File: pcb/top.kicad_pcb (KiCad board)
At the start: 2 copper layers, 186 x 28 mm, 66 parts, among them J1 Conn_01x01, J10 Conn_01x01, J11 Conn_01x01, J2 Conn_01x01, J3 Conn_01x06, J4 Conn_01x01, J5 Conn_01x01, J6 Conn_01x01, J7 Conn_01x01, J8 Conn_01x01, J9 Conn_01x01, Q1 2N7002, Q2 2N7002, Q3 2N7002, Q4 2N7002, U1 L78L05_SOT89, U2 PIC12F629-ISN

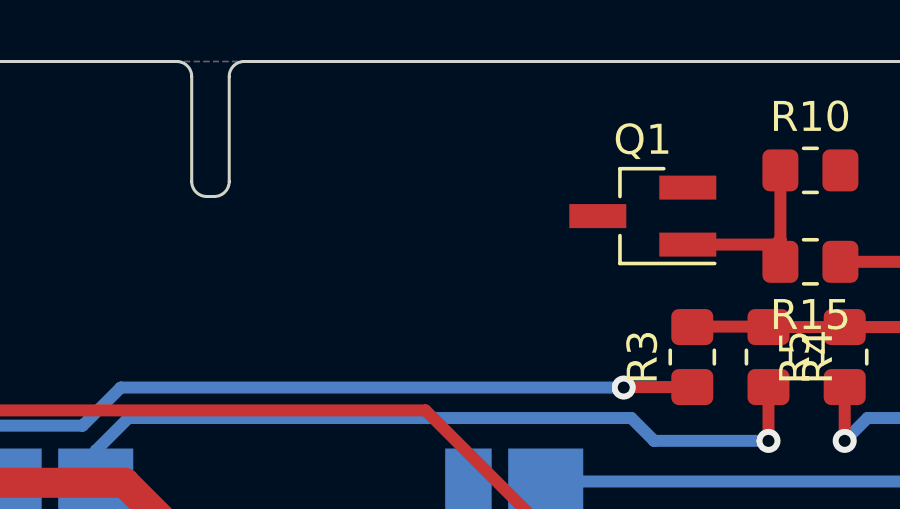
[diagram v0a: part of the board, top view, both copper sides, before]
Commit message: Add load resistor for CV reading.
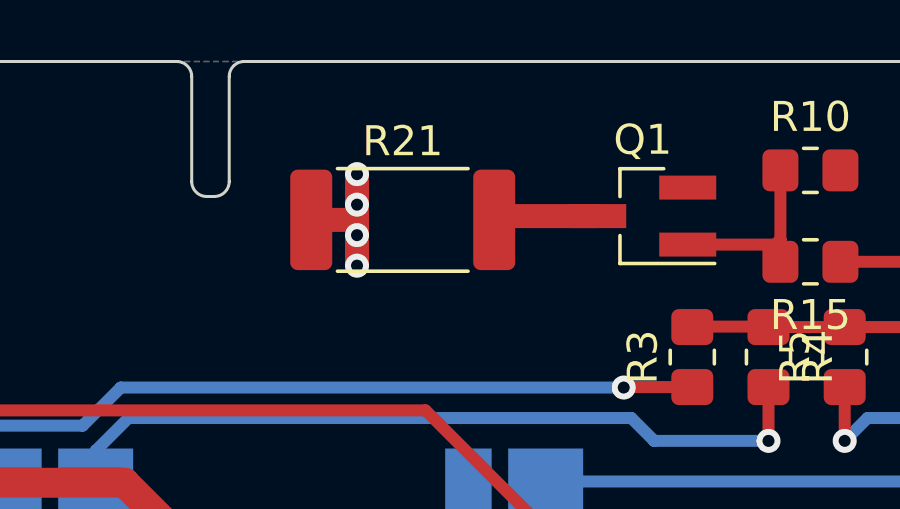
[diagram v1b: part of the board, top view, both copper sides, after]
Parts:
- added R21: 220R, Resistor_SMD:R_2512_6332Metric_Pad1.40x3.35mm_HandSolder, F.Cu at (113.3, 81.3)
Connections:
- Q1 pad 3: unconnected-(Q1-Pad3) -> Net-(Q1-Pad3)
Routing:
- net +15V: track 37.2 -> 41.8 mm, vias 14 -> 18
- net Net-(Q1-Pad3): track 0.00 -> 3.50 mm

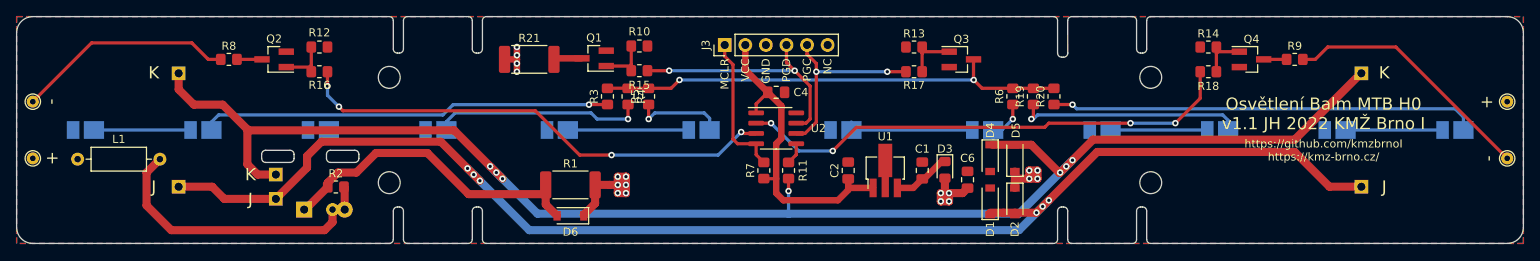
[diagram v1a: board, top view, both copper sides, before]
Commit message: Use 8V stabilized for LEDs.
To keep LEDs longer running on capacitor while maintaining brightness.
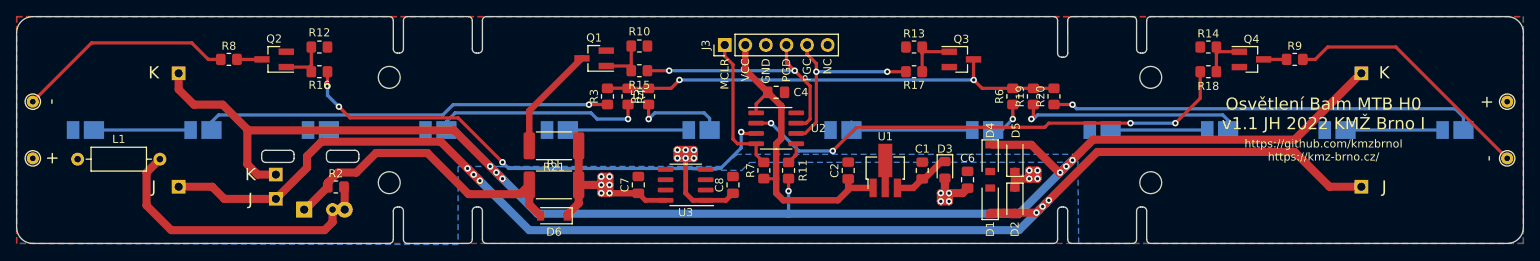
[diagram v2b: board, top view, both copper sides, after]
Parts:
- added C7: 22u/25V, Capacitor_SMD:C_0805_2012Metric_Pad1.18x1.45mm_HandSolder, F.Cu at (126.7, 96.8)
- added C8: 22u/25V, Capacitor_SMD:C_0805_2012Metric_Pad1.18x1.45mm_HandSolder, F.Cu at (138.4, 96.8)
- added U3: L78L08_SO8, Package_SO:SOIC-8_3.9x4.9mm_P1.27mm, F.Cu at (132.6, 96.8)
- R19, R20, R3, R4, R5, R6: value 10k -> 2k2
- moved R21 11.1 mm to (116.3, 91.9), turned to 180 degrees
- moved D6 2.03 mm to (116.3, 100.6)
- moved R1 2.03 mm to (116.3, 96.8)
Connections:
- D11 pad 2: +15V -> +8V
- D12 pad 2: +15V -> +8V
- D15 pad 2: +15V -> +8V
- D16 pad 2: +15V -> +8V
- D7 pad 2: +15V -> +8V
- D8 pad 2: +15V -> +8V
- J6 pad 1: +15V -> +8V
- J7 pad 1: +15V -> +8V
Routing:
- net +8V: track 0.00 -> 20.4 mm, vias 0 -> 6
- net Net-(Q1-Pad3): track 3.50 -> 13.5 mm
- net +15V: track 41.8 -> 48.8 mm, vias 18 -> 14
- net Net-(R16-Pad1): track 60.1 -> 62.6 mm
- net Net-(R2-Pad1): track 39.2 -> 37.9 mm
- added copper zone on B.Cu, net +8V

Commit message: Tweak silkscreen.
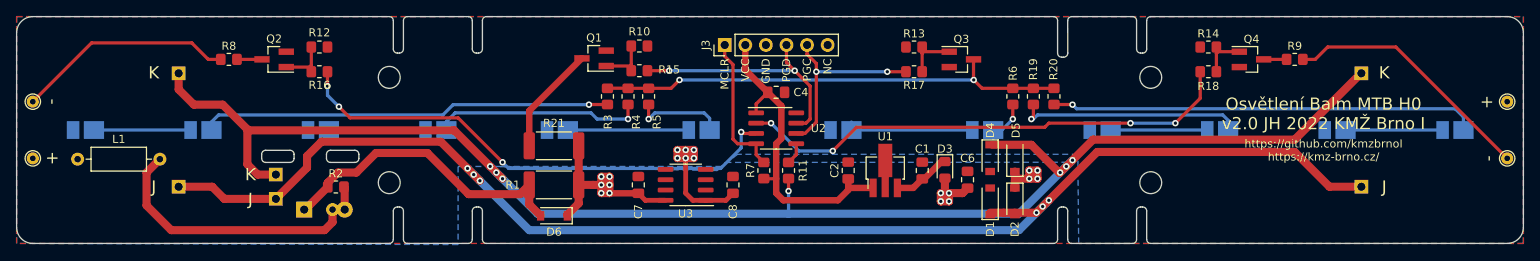
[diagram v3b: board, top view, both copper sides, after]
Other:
- board text added: "Osvětlení Balm MTB H0 v2.0 JH 2022 KMŽ Brno I"
- board text removed: "Osvětlení Balm MTB H0 v1.1 JH 2022 KMŽ Brno I"
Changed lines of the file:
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@@
     (property "Sheetname" "")
     (attr smd)
-    (fp_text reference "R1" (at 0 -2.62) (layer "F.SilkS")
+    (fp_text reference "R1" (at -5.08 0) (layer "F.SilkS")
       (effects (font (size 1 1) (thickness 0.15)))
     )
@@
     (property "Sheetname" "")
     (attr smd)
-    (fp_text reference "R15" (at 0 1.778) (layer "F.SilkS")
+    (fp_text reference "R15" (at 3.683 -0.127) (layer "F.SilkS")
       (effects (font (size 1 1) (thickness 0.15)))
     )
@@
     (property "Sheetname" "")
     (attr smd)
-    (fp_text reference "R4" (at 0 1.651 90) (layer "F.SilkS")
+    (fp_text reference "R4" (at -3.148 1.016 90) (layer "F.SilkS")
       (effects (font (size 1 1) (thickness 0.15)))
     )
@@
     (property "Sheetname" "")
     (attr smd)
-    (fp_text reference "R3" (at 0 -1.65 90) (layer "F.SilkS")
+    (fp_text reference "R3" (at -3.148 0.064 90) (layer "F.SilkS")
       (effects (font (size 1 1) (thickness 0.15)))
     )
@@
     (property "Sheetname" "")
     (attr smd)
-    (fp_text reference "R6" (at 0 -1.65 90) (layer "F.SilkS")
+    (fp_text reference "R6" (at 2.852 0.026 90) (layer "F.SilkS")
       (effects (font (size 1 1) (thickness 0.15)))
     )
@@
     (property "Sheetname" "")
     (attr smd)
-    (fp_text reference "C7" (at 0 -1.68 90) (layer "F.SilkS")
+    (fp_text reference "C7" (at -3.302 0 90) (layer "F.SilkS")
       (effects (font (size 1 1) (thickness 0.15)))
     )
@@
     (property "Sheetname" "")
     (attr smd)
-    (fp_text reference "C8" (at 0 -1.68 90) (layer "F.SilkS")
+    (fp_text reference "C8" (at -3.302 0 90) (layer "F.SilkS")
       (effects (font (size 1 1) (thickness 0.15)))
     )
@@
     (property "Sheetname" "")
     (attr smd)
-    (fp_text reference "R20" (at 0 -1.65 90) (layer "F.SilkS")
+    (fp_text reference "R20" (at 3.352 -0.054 90) (layer "F.SilkS")
       (effects (font (size 1 1) (thickness 0.15)))
     )
@@
     (property "Sheetname" "")
     (attr smd)
-    (fp_text reference "R5" (at 0 -1.65 90) (layer "F.SilkS")
+    (fp_text reference "R5" (at -3.148 1.016 90) (layer "F.SilkS")
       (effects (font (size 1 1) (thickness 0.15)))
     )
@@
     (property "Sheetname" "")
     (attr smd)
-    (fp_text reference "R21" (at 0 -2.62) (layer "F.SilkS")
+    (fp_text reference "R21" (at 0 2.794) (layer "F.SilkS")
       (effects (font (size 1 1) (thickness 0.15)))
     )
@@
     (property "Sheetname" "")
     (attr smd)
-    (fp_text reference "R19" (at 0 -1.65 90) (layer "F.SilkS")
+    (fp_text reference "R19" (at 3.352 -0.014 90) (layer "F.SilkS")
       (effects (font (size 1 1) (thickness 0.15)))
     )
@@
     (property "Sheetname" "")
     (attr smd)
-    (fp_text reference "U3" (at 0 -3.4) (layer "F.SilkS")
+    (fp_text reference "U3" (at 0 -3.556) (layer "F.SilkS")
       (effects (font (size 1 1) (thickness 0.15)))
     )
@@
     (effects (font (size 1 1) (thickness 0.15)) (justify right))
   )
-  (gr_text "Osvětlení Balm MTB H0\nv1.1 JH 2022 KMŽ Brno I" (at 211.328 88) (layer "F.SilkS")
+  (gr_text "Osvětlení Balm MTB H0\nv2.0 JH 2022 KMŽ Brno I" (at 211.328 88) (layer "F.SilkS")
     (effects (font (size 1.5 1.5) (thickness 0.15)))
   )
@@
         (xy 114 100)
         (xy 108.5 94.5)
-        (xy 139.5 95)
-        (xy 140.5 94)
+        (xy 136.5 95)
+        (xy 137.5 94)
         (xy 180.086 93.98)
       )

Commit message: Add holes for wires.
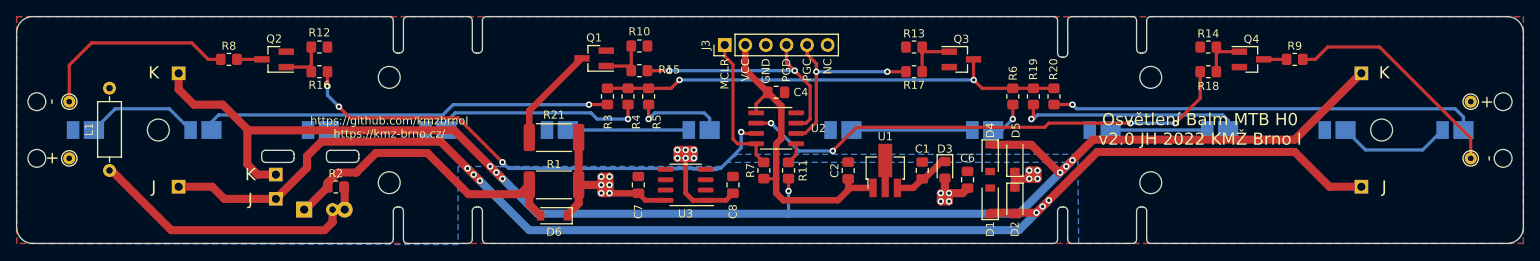
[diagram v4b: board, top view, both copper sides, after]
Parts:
- added H10: MountingHole, MountingHole:MountingHole_2.2mm_M2, F.Cu at (52.5, 93.5)
- added H5: MountingHole, MountingHole:MountingHole_2.7mm_M2.5, F.Cu at (218.5, 90.0)
- added H6: MountingHole, MountingHole:MountingHole_2.7mm_M2.5, F.Cu at (67.5, 90.0)
- added H7: MountingHole, MountingHole:MountingHole_2.2mm_M2, F.Cu at (233.5, 86.5)
- added H8: MountingHole, MountingHole:MountingHole_2.2mm_M2, F.Cu at (233.5, 93.5)
- added H9: MountingHole, MountingHole:MountingHole_2.2mm_M2, F.Cu at (52.5, 86.5)
- moved L1 9.61 mm to (61.5, 84.8), turned to -90 degrees
- moved J6 4.50 mm to (56.5, 93.5)
- moved J7 4.50 mm to (229.5, 86.5)
- moved J8 4.50 mm to (56.5, 86.5)
- moved J9 4.50 mm to (229.5, 93.5)
- moved R21 1.02 mm to (116.3, 90.9)
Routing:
- net Net-(J9-Pad1): track 31.6 -> 28.5 mm
- net Net-(D7-Pad1): track 11.9 -> 14.1 mm
- net Net-(D16-Pad1): track 12.0 -> 14.0 mm
- net Net-(J8-Pad1): track 27.0 -> 25.2 mm
- net Net-(D10-Pad1): track 5.83 -> 4.78 mm
- net Net-(Q1-Pad3): track 13.5 -> 12.5 mm
- net +15V: track 48.8 -> 49.8 mm
- net Net-(D10-Pad2): track 15.9 -> 14.9 mm
- net +8V: track 20.4 -> 19.9 mm

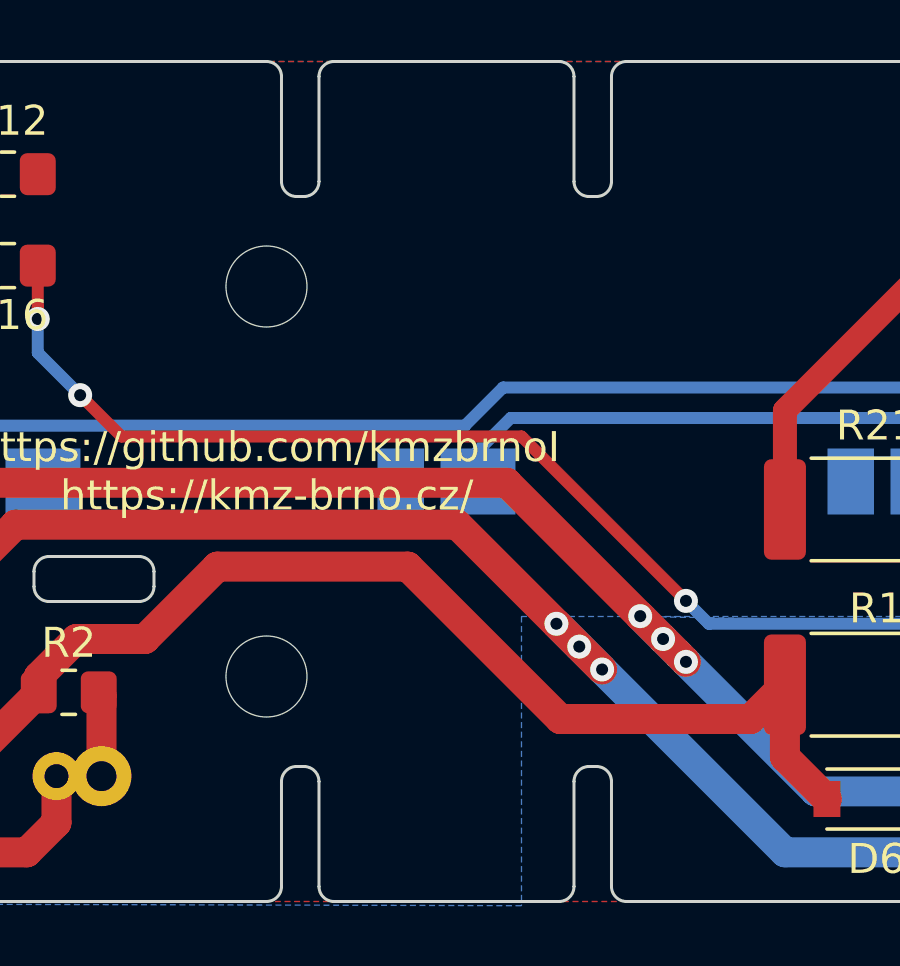
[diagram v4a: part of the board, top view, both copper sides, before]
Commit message: Add oshw & weee logos.
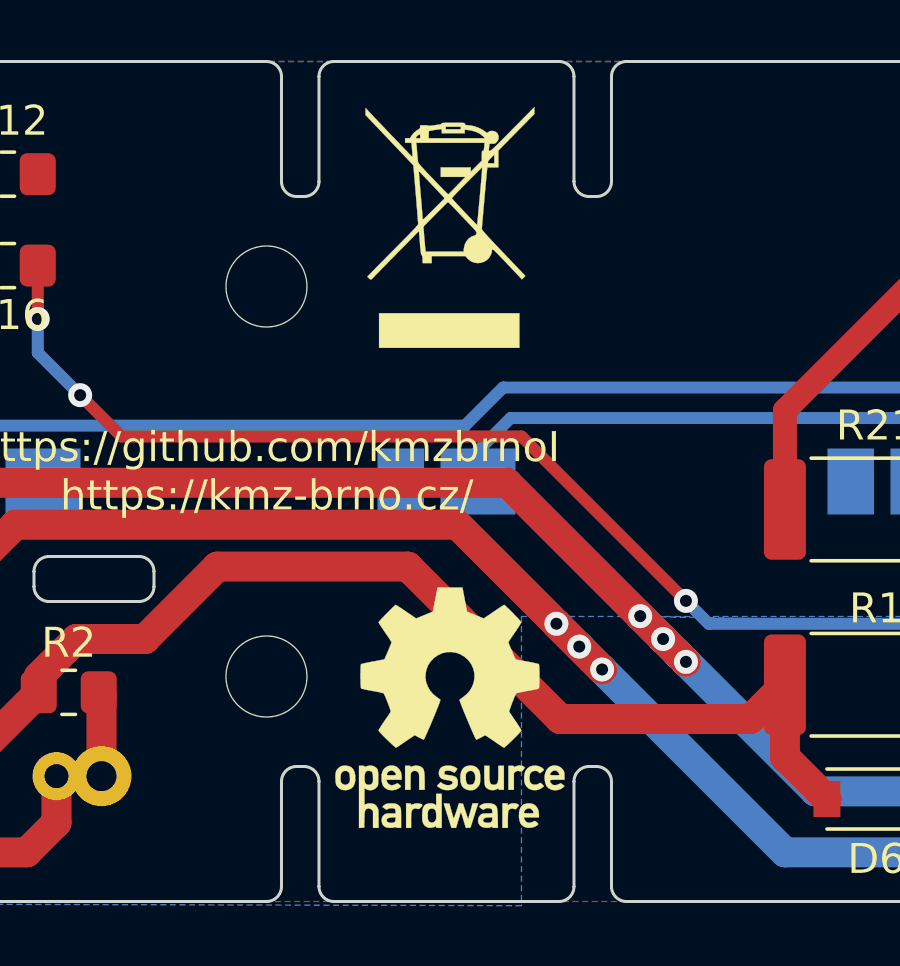
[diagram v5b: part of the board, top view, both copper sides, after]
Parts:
- added REF**: WEEE-Logo_5.6x8mm_SilkScreen, Symbol:WEEE-Logo_5.6x8mm_SilkScreen, F.Cu at (102.1, 81.5)
- added REF**: OSHW-Logo_7.5x8mm_SilkScreen, Symbol:OSHW-Logo_7.5x8mm_SilkScreen, F.Cu at (102.1, 97.5)
